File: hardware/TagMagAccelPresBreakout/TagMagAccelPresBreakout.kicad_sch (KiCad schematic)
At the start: 28 parts, among them J1 Conn_01x06, J2 Conn_01x04, J3 Conn_01x04, J4 Conn_01x06, J401 CONN_01X02, J5 Conn_01x06, Q501 Q_NPN_BEC, U1 at25ff321D-UUN, U2 LIS2DU12TR, U3 LPS27HHWTR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

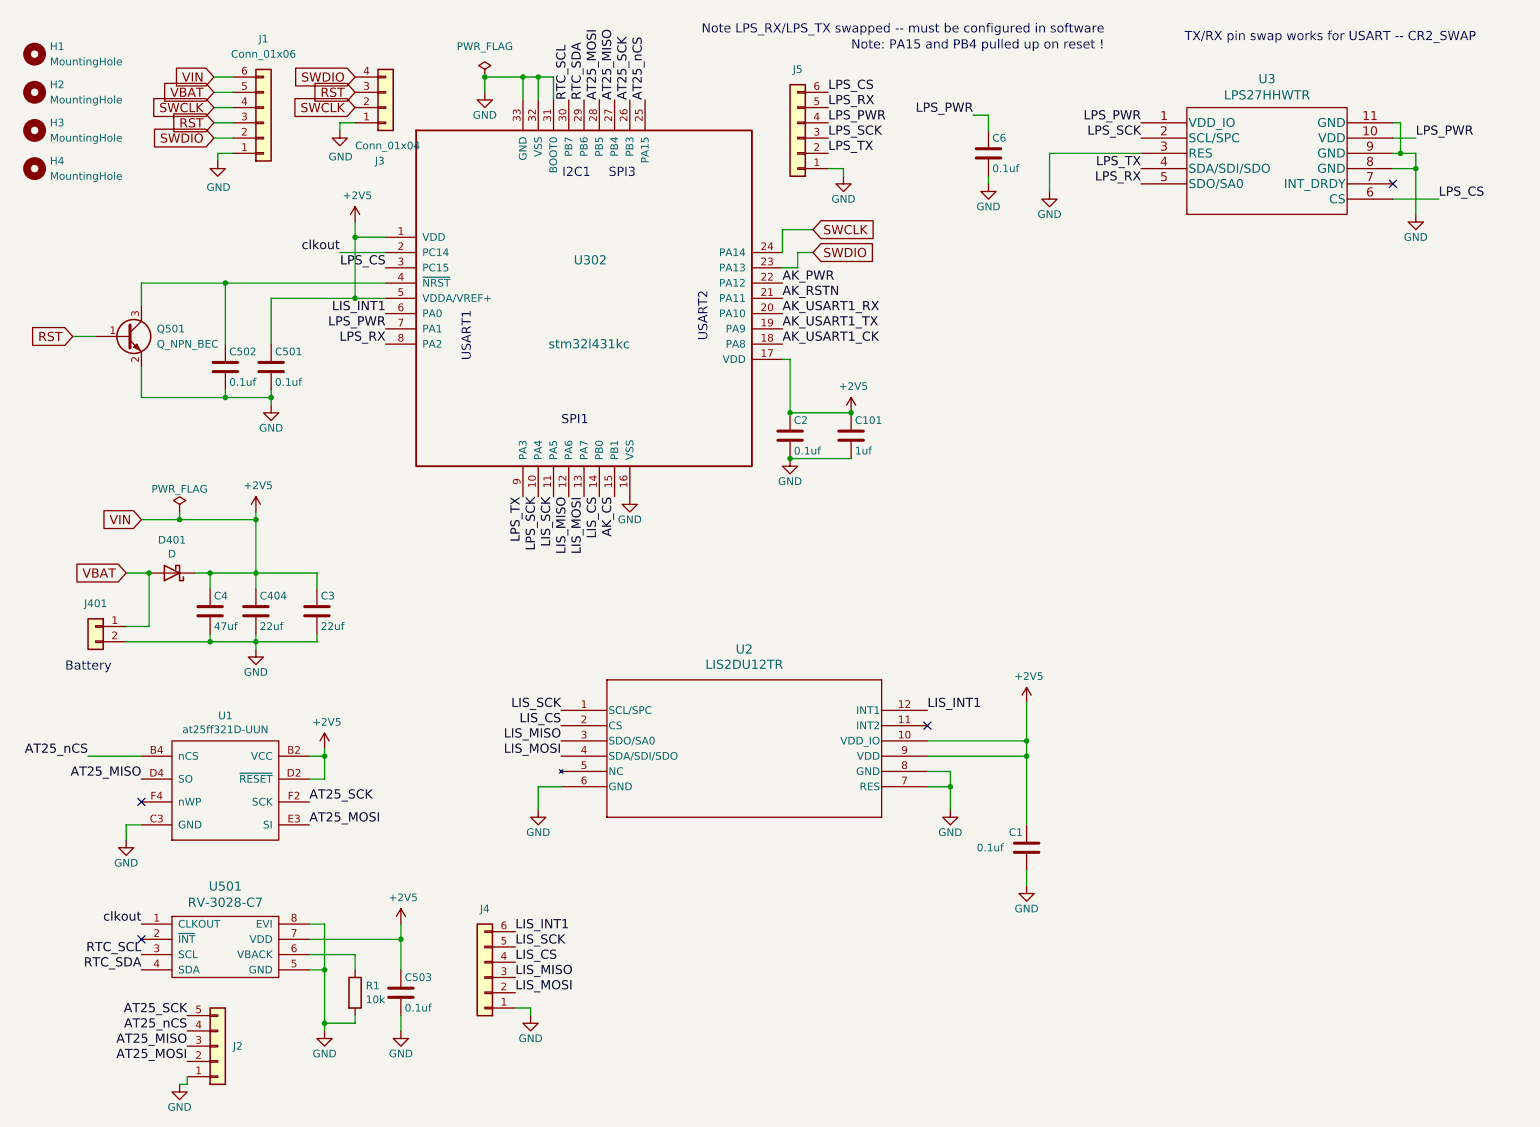
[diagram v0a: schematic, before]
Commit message: finish breakout board with mag, accel, pres
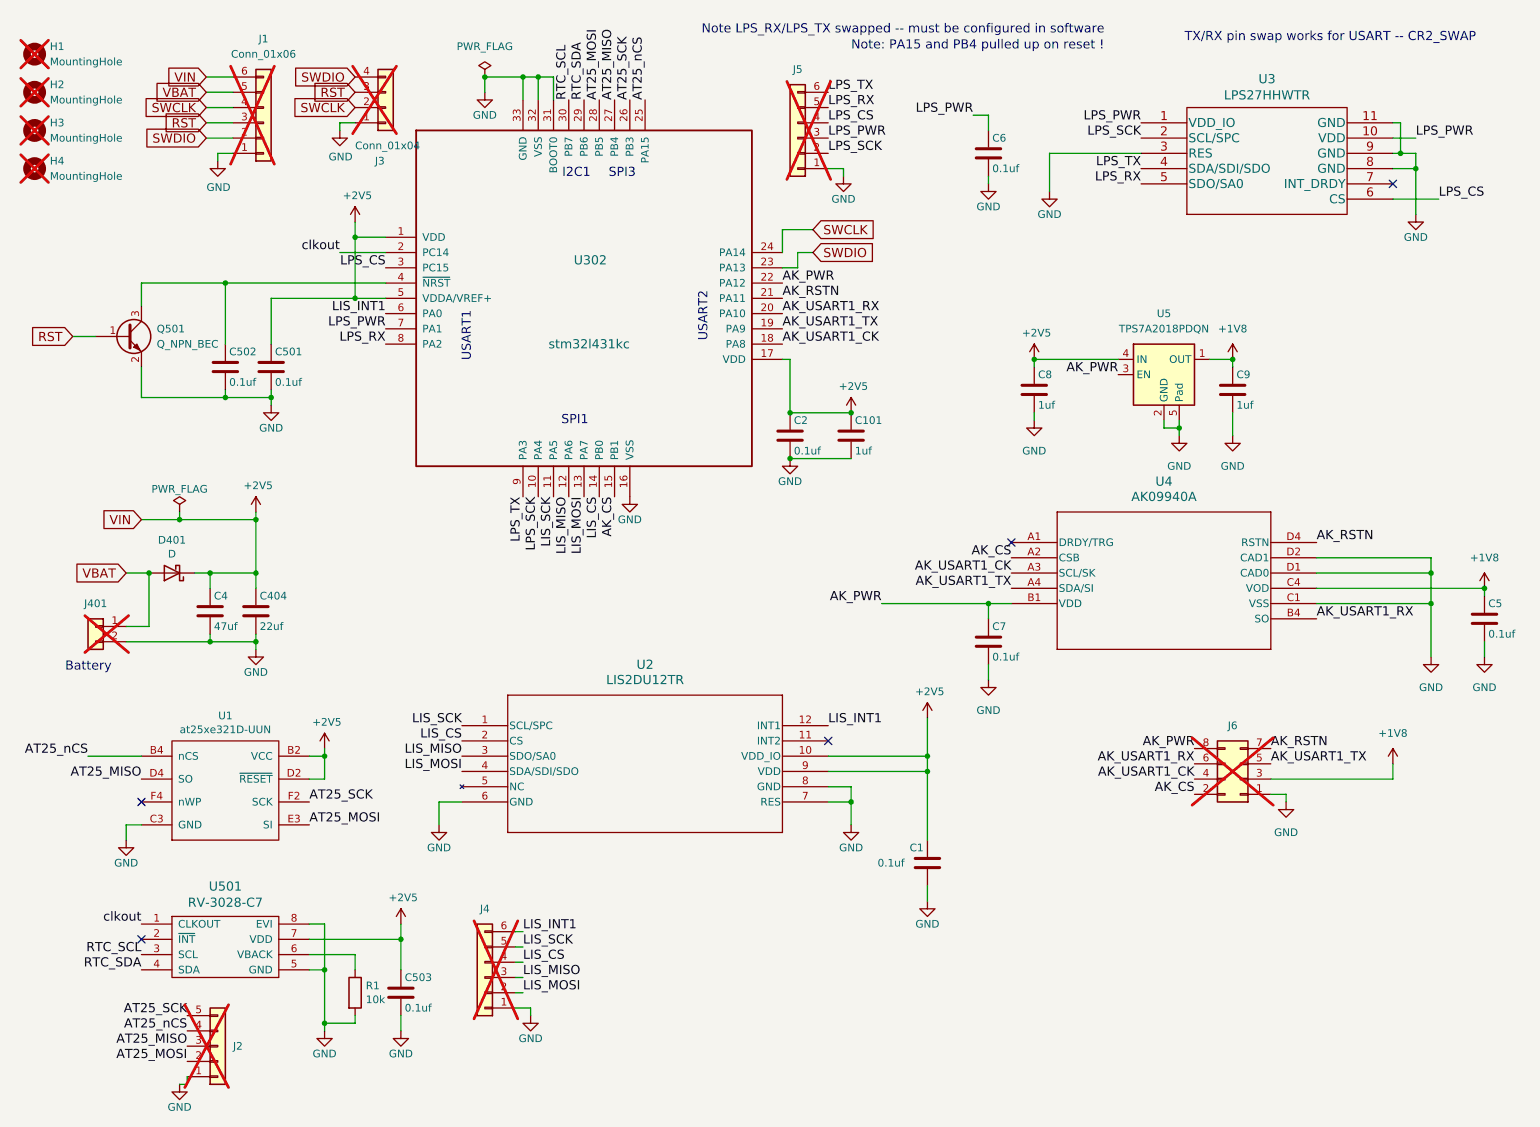
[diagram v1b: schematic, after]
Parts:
- removed C3: 22uf, Capacitor_SMD:C_0402_1005Metric, symbol Device:C
- added C5, C7: 0.1uf, Capacitor_SMD:C_0201_0603Metric, symbol Device:C
- added C8, C9: 1uf, Capacitor_SMD:C_0201_0603Metric, symbol Device:C
- added J6: Conn_02x04_Counter_Clockwise, Connector_PinHeader_2.54mm:PinHeader_2x04_P2.54mm_Vertical, symbol Connector_Generic:Conn_02x04_Odd_Even
- added U4: AK09940A, library:AK09940a, symbol ak09940a:AK09940A
- added U5: TPS7A2018PDQN, Package_SON:Texas_X2SON-4_1x1mm_P0.65mm, symbol Regulator_Linear:TPS7A20xxxDQN
- C1: MPN C181047 -> GRM033C81E104KE14D
- H1, H2, H3, H4, J1, J2, J3, J4, J401, J5: now not fitted
- U1: value at25ff321D-UUN -> at25xe321D-UUN; MFN Dialog -> Renesas; MPN AT25FF321A-UUN-T (Mouser) -> AT25XE321D-UUN-T
- U2: DISTPN (none) -> 497-LIS2DU12TRCT-ND; MFN (none) -> STMicroelectronics; MPN (none) -> LIS2DU12TR
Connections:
- net +2V5: now also C8.1, U5.4 (IN)
- net AK_CS: now also J6.2 (Pin_2), U4.A2 (CSB)
- net AK_PWR: now also C7.1, J6.8 (Pin_8), U4.B1 (VDD), U5.3 (EN)
- net AK_RSTN: now also J6.7 (Pin_7), U4.D4 (RSTN)
- net AK_USART1_CK: now also J6.4 (Pin_4), U4.A3 (SCL/SK)
- net AK_USART1_RX: now also J6.6 (Pin_6), U4.B4 (SO)
- net AK_USART1_TX: now also J6.5 (Pin_5), U4.A4 (SDA/SI)
- net GND: now also C5.2, C7.2, C8.2, C9.2, J6.1 (Pin_1), U4.C1 (VSS), U4.D1 (CAD0), U4.D2 (CAD1), U5.2 (GND), U5.5 (Pad)
- net LPS_CS: now also J5.4 (Pin_4); no longer J5.6 (Pin_6)
- net LPS_PWR: now also J5.3 (Pin_3); no longer J5.4 (Pin_4)
- net LPS_SCK: now also J5.2 (Pin_2); no longer J5.3 (Pin_3)
- net LPS_TX: now also J5.6 (Pin_6); no longer J5.2 (Pin_2)
- new net +1V8: C5.1, C9.1, J6.3 (Pin_3), U4.C4 (VOD), U5.1 (OUT)
- no-connect marks 4 -> 5
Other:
- moved on the sheet: C1, U2

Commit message: checkpoint
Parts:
- H1, H2, H3, H4: now fitted
- J1, J2, J3, J4, J401, J5, J6: now fitted; now left out of the parts list
- U2: footprint library:LGA-12L_LIS2DU12_STM -> LGA-12L_LIS2DU12_STM; symbol lis2du12:LIS2DU12TR -> lis2du12tr:LIS2DU12TR

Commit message: designed compass tag
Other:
- note added: "WARNING -- POWER LINES REVERSED on AK09940A"
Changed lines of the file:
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@@
+		)
+	)
+	(text "WARNING -- POWER LINES REVERSED on\nAK09940A"
+		(exclude_from_sim no)
+		(at 210.82 123.825 0)
+		(effects
+			(font
+				(size 1.524 1.524)
+				(color 255 25 71 1)
+			)
 		)
 	)
